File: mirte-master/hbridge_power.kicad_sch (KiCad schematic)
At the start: 2 parts, among them J22 hbridge_1, J23 hbridge_2

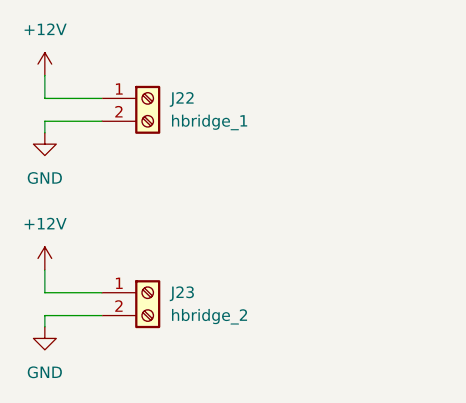
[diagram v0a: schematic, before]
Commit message: add kerco/elcos
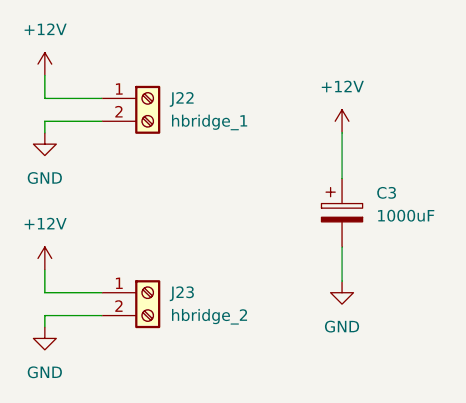
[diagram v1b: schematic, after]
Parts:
- added C3: 1000uF, Capacitor_THT:CP_Radial_D10.0mm_P3.50mm, symbol Device:C_Polarized
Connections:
- net +12V: now also C3.1
- net GND: now also C3.2
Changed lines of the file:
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@@
+    (stroke (width 0) (type default))
+  )
+  (wire (pts (xy 138.43 76.2) (xy 138.43 81.28))
     (stroke (width 0) (type default))
   )
@@
     (stroke (width 0) (type default))
   )
+  (wire (pts (xy 138.43 88.9) (xy 138.43 92.71))
+    (stroke (width 0) (type default))
+  )
   (wire (pts (xy 105.41 97.79) (xy 105.41 96.52))
     (stroke (width 0) (type default))
@@
     )
   )
+  (symbol (lib_id "power:+12V") (at 138.43 76.2 0) (unit 1)
+    (in_bom yes) (on_board yes) (dnp no) (fields_autoplaced)
+    (property "Reference" "#PWR013" (at 138.43 80.01 0)
+      (effects (font (size 1.27 1.27)) hide)
+    )
+    (property "Value" "+12V" (at 138.43 71.12 0)
+      (effects (font (size 1.27 1.27)))
+    )
+    (property "Footprint" "" (at 138.43 76.2 0)
+      (effects (font (size 1.27 1.27)) hide)
+    )
+    (property "Datasheet" "" (at 138.43 76.2 0)
+      (effects (font (size 1.27 1.27)) hide)
+    )
+    (pin "1")
+    (instances
+      (project "mirte-master"
+        (path "/19794465-0368-488c-958e-83b02754ebd6/17ebe4c8-09bb-4699-976c-396d27e4a3f5/cd5c3f96-e789-467d-9a0a-1e1e5a42c039"
+          (reference "#PWR013") (unit 1)
+        )
+      )
+    )
+  )
   (symbol (lib_id "Connector:Screw_Terminal_01x02") (at 116.84 72.39 0) (unit 1)
     (in_bom yes) (on_board yes) (dnp no) (fields_autoplaced)
@@
         )
       )
+    )
+  )
+  (symbol (lib_id "Device:C_Polarized") (at 138.43 85.09 0) (unit 1)
+    (in_bom yes) (on_board yes) (dnp no) (fields_autoplaced)
+    (property "Reference" "C3" (at 142.24 82.931 0)
+      (effects (font (size 1.27 1.27)) (justify left))
+    )
+    (property "Value" "1000uF" (at 142.24 85.471 0)
+      (effects (font (size 1.27 1.27)) (justify left))
+    )
+    (property "Footprint" "Capacitor_THT:CP_Radial_D10.0mm_P3.50mm" (at 139.3952 88.9 0)
+      (effects (font (size 1.27 1.27)) hide)
+    )
+    (property "Datasheet" "~" (at 138.43 85.09 0)
+      (effects (font (size 1.27 1.27)) hide)
+    )
+    (pin "1")
+    (pin "2")
+    (instances
+      (project "mirte-master"
+        (path "/19794465-0368-488c-958e-83b02754ebd6/17ebe4c8-09bb-4699-976c-396d27e4a3f5/cd5c3f96-e789-467d-9a0a-1e1e5a42c039"
+          (reference "C3") (unit 1)
+        )
+      )
+    )
+  )
+  (symbol (lib_id "power:GND") (at 138.43 92.71 0) (unit 1)
+    (in_bom yes) (on_board yes) (dnp no) (fields_autoplaced)
+    (property "Reference" "#PWR064" (at 138.43 99.06 0)
+      (effects (font (size 1.27 1.27)) hide)
+    )
+    (property "Value" "GND" (at 138.43 97.79 0)
+      (effects (font (size 1.27 1.27)))
+    )
+    (property "Footprint" "" (at 138.43 92.71 0)
+      (effects (font (size 1.27 1.27)) hide)
+    )
+    (property "Datasheet" "" (at 138.43 92.71 0)
+      (effects (font (size 1.27 1.27)) hide)
+    )
+    (pin "1")
+    (instances
+      (project "mirte-master"
+        (path "/19794465-0368-488c-958e-83b02754ebd6/17ebe4c8-09bb-4699-976c-396d27e4a3f5/cd5c3f96-e789-467d-9a0a-1e1e5a42c039"
+          (reference "#PWR064") (unit 1)
+        )
+      )

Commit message: mirte master parts jclpcb fixed
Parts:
- removed J22: hbridge_1, easyeda:CONN-TH_XY126V-5.0-2P, symbol Connector:Screw_Terminal_01x02
- removed J23: hbridge_2, easyeda:CONN-TH_XY126V-5.0-2P, symbol Connector:Screw_Terminal_01x02
- added J16, J19: sc, easyeda:CONN-TH_XY126V-5.0-2P, symbol Connector:Screw_Terminal_01x02
- C3: LCSC (none) -> C110138
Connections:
- net +12V: now also J16.1 (Pin_1), J19.1 (Pin_1)
- net GND: now also J16.2 (Pin_2), J19.2 (Pin_2)
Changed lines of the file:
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@@
+    )
+  )
+  (symbol (lib_id "Connector:Screw_Terminal_01x02") (at 116.84 72.39 0) (unit 1)
+    (in_bom yes) (on_board yes) (dnp no) (fields_autoplaced)
+    (property "Reference" "J19" (at 119.38 72.39 0)
+      (effects (font (size 1.27 1.27)) (justify left))
+    )
+    (property "Value" "sc" (at 119.38 74.93 0)
+      (effects (font (size 1.27 1.27)) (justify left))
+    )
+    (property "Footprint" "easyeda:CONN-TH_XY126V-5.0-2P" (at 116.84 72.39 0)
+      (effects (font (size 1.27 1.27)) hide)
+    )
+    (property "Datasheet" "~" (at 116.84 72.39 0)
+      (effects (font (size 1.27 1.27)) hide)
+    )
+    (property "LCSC" "C557646" (at 116.84 72.39 0)
+      (effects (font (size 1.27 1.27)) hide)
+    )
+    (pin "2")
+    (pin "1")
+    (instances
+      (project "mirte-master"
+        (path "/19794465-0368-488c-958e-83b02754ebd6/17ebe4c8-09bb-4699-976c-396d27e4a3f5/cd5c3f96-e789-467d-9a0a-1e1e5a42c039"
+          (reference "J19") (unit 1)
+        )
+        (path "/19794465-0368-488c-958e-83b02754ebd6/17ebe4c8-09bb-4699-976c-396d27e4a3f5/1f6ba3bd-b93c-4e80-aba0-1409dab869f7"
+          (reference "J13") (unit 1)
+        )
+      )
     )
   )
@@
     )
   )
-  (symbol (lib_id "Connector:Screw_Terminal_01x02") (at 116.84 72.39 0) (unit 1)
+  (symbol (lib_id "Connector:Screw_Terminal_01x02") (at 116.84 93.98 0) (unit 1)
     (in_bom yes) (on_board yes) (dnp no) (fields_autoplaced)
-    (property "Reference" "J22" (at 119.38 72.39 0)
+    (property "Reference" "J16" (at 119.38 93.98 0)
       (effects (font (size 1.27 1.27)) (justify left))
     )
-    (property "Value" "hbridge_1" (at 119.38 74.93 0)
-      (effects (font (size 1.27 1.27)) (justify left))
-    )
-    (property "Footprint" "easyeda:CONN-TH_XY126V-5.0-2P" (at 116.84 72.39 0)
-      (effects (font (size 1.27 1.27)) hide)
-    )
-    (property "Datasheet" "~" (at 116.84 72.39 0)
-      (effects (font (size 1.27 1.27)) hide)
-    )
-    (property "LCSC" "C557646" (at 116.84 72.39 0)
-      (effects (font (size 1.27 1.27)) hide)
-    )
-    (pin "2")
-    (pin "1")
-    (instances
-      (project "mirte-master"
-        (path "/19794465-0368-488c-958e-83b02754ebd6/17ebe4c8-09bb-4699-976c-396d27e4a3f5/cd5c3f96-e789-467d-9a0a-1e1e5a42c039"
-          (reference "J22") (unit 1)
-        )
-      )
-    )
-  )
-  (symbol (lib_id "Connector:Screw_Terminal_01x02") (at 116.84 93.98 0) (unit 1)
-    (in_bom yes) (on_board yes) (dnp no) (fields_autoplaced)
-    (property "Reference" "J23" (at 119.38 93.98 0)
-      (effects (font (size 1.27 1.27)) (justify left))
-    )
-    (property "Value" "hbridge_2" (at 119.38 96.52 0)
+    (property "Value" "sc" (at 119.38 96.52 0)
       (effects (font (size 1.27 1.27)) (justify left))
     )
@@
       (project "mirte-master"
         (path "/19794465-0368-488c-958e-83b02754ebd6/17ebe4c8-09bb-4699-976c-396d27e4a3f5/cd5c3f96-e789-467d-9a0a-1e1e5a42c039"
-          (reference "J23") (unit 1)
+          (reference "J16") (unit 1)
+        )
+        (path "/19794465-0368-488c-958e-83b02754ebd6/17ebe4c8-09bb-4699-976c-396d27e4a3f5/1f6ba3bd-b93c-4e80-aba0-1409dab869f7"
+          (reference "J13") (unit 1)
         )
       )
@@
       (effects (font (size 1.27 1.27)) hide)
     )
+    (property "LCSC" "C110138" (at 138.43 85.09 0)
+      (effects (font (size 1.27 1.27)) hide)
+    )

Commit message: mirte-master schematic cleanup and readabilityimprovements
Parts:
- removed C3: 1000uF, Capacitor_THT:CP_Radial_D10.0mm_P3.50mm, symbol Device:C_Polarized
- removed J16, J19: sc, easyeda:CONN-TH_XY126V-5.0-2P, symbol Connector:Screw_Terminal_01x02
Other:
- title: (none) -> ${PROJECTNAME}
